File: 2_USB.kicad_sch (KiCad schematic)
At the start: 9 parts, among them J301 USB_C_Receptacle_USB2.0_16P, J302 Conn_02x03_Row_Letter_First, U301 CH224K, U302 FSUSB42MUX

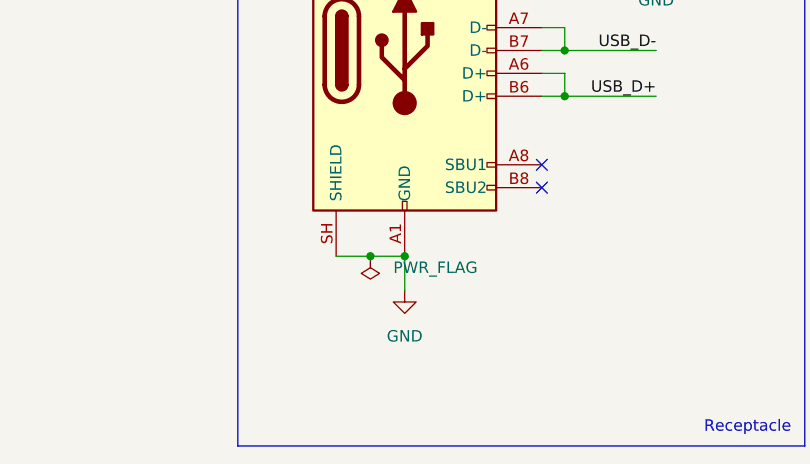
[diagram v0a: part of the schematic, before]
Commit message: Added hardware switch for active control Also added a coupling capacitor between receptacle shells and reference ground Added some more notes
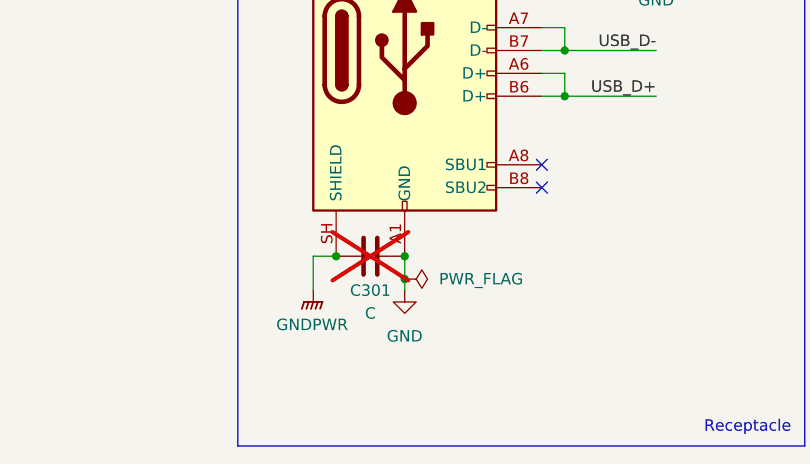
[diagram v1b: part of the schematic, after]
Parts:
- added C301: C, symbol Device:C
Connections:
- net GND: now also C301.2; no longer J301.SH (SHIELD)
- new net GNDPWR: C301.1, J301.SH (SHIELD)
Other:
- title: (none) -> Polaris/USB
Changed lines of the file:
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@@
 	(generator_version "10.0")
 	(paper "A4")
+	(title_block
+		(title "Polaris/USB")
+	)
 	(rectangle
 		(start 104.648 69.85)
@@
 			)
 		)
-	)
-	(junction
-		(at 53.34 125.73)
-		(diameter 0)
-		(color 0 0 0 0)
 	)
 	(junction
@@
 	)
 	(junction
-		(at 87.63 85.09)
+		(at 49.53 125.73)
 		(diameter 0)
 		(color 0 0 0 0)
@@
 	)
 	(junction
+		(at 87.63 85.09)
+		(diameter 0)
+		(color 0 0 0 0)
+	)
+	(junction
 		(at 144.78 128.27)
 		(diameter 0)
@@
 	)
 	(junction
+		(at 57.15 128.27)
+		(diameter 0)
+		(color 0 0 0 0)
+	)
+	(junction
 		(at 144.78 130.81)
 		(diameter 0)
@@
 	(wire
 		(pts
+			(xy 46.99 129.54) (xy 46.99 125.73)
+		)
+		(stroke
+			(width 0)
+			(type default)
+		)
+	)
+	(wire
+		(pts
+			(xy 57.15 128.27) (xy 57.15 129.54)
+		)
+		(stroke
+			(width 0)
+			(type default)
+		)
+	)
+	(wire
+		(pts
 			(xy 142.24 125.73) (xy 144.78 125.73)
 		)
@@
 	(wire
 		(pts
-			(xy 53.34 125.73) (xy 57.15 125.73)
-		)
-		(stroke
-			(width 0)
-			(type default)
-		)
-	)
-	(wire
-		(pts
 			(xy 72.39 105.41) (xy 74.93 105.41)
 		)
@@
 	(wire
 		(pts
-			(xy 49.53 125.73) (xy 53.34 125.73)
-		)
-		(stroke
-			(width 0)
-			(type default)
-		)
-	)
-	(wire
-		(pts
 			(xy 72.39 85.09) (xy 85.09 85.09)
 		)
@@
 	(wire
 		(pts
-			(xy 57.15 125.73) (xy 57.15 129.54)
+			(xy 57.15 125.73) (xy 57.15 128.27)
 		)
 		(stroke
@@
 		(pts
 			(xy 144.78 128.27) (xy 144.78 130.81)
+		)
+		(stroke
+			(width 0)
+			(type default)
+		)
+	)
+	(wire
+		(pts
+			(xy 46.99 125.73) (xy 49.53 125.73)
 		)
 		(stroke
@@
 	(symbol
 		(lib_id "power:PWR_FLAG")
-		(at 53.34 125.73 180)
+		(at 57.15 128.27 270)
 		(unit 1)
 		(body_style 1)
@@
 		(fields_autoplaced yes)
 		(property "Reference" "#FLG0302"
-			(at 53.34 127.635 0)
+			(at 59.055 128.27 0)
 			(hide yes)
 			(show_name no)
@@
 		)
 		(property "Value" "PWR_FLAG"
-			(at 55.88 126.9999 0)
-			(show_name no)
-			(do_not_autoplace no)
-			(effects
-				(font
-					(size 1.27 1.27)
-				)
-				(justify right)
+			(at 60.96 128.2699 90)
+			(show_name no)
+			(do_not_autoplace no)
+			(effects
+				(font
+					(size 1.27 1.27)
+				)
+				(justify left)
 			)
 		)
 		(property "Footprint" ""
-			(at 53.34 125.73 0)
+			(at 57.15 128.27 0)
 			(hide yes)
 			(show_name no)
@@
 		)
 		(property "Datasheet" ""
-			(at 53.34 125.73 0)
+			(at 57.15 128.27 0)
 			(hide yes)
 			(show_name no)
@@
 		)
 		(property "Description" "Special symbol for telling ERC where power comes from"
-			(at 53.34 125.73 0)
+			(at 57.15 128.27 0)
 			(hide yes)
 			(show_name no)
@@
 	)
 	(symbol
+		(lib_id "power:GNDPWR")
+		(at 46.99 129.54 0)
+		(unit 1)
+		(body_style 1)
+		(exclude_from_sim no)
+		(in_bom yes)
+		(on_board yes)
+		(in_pos_files yes)
+		(dnp no)
+		(fields_autoplaced yes)
+		(property "Reference" "#PWR0310"
+			(at 46.99 134.62 0)
+			(hide yes)
+			(show_name no)
+			(do_not_autoplace no)
+			(effects
+				(font
+					(size 1.27 1.27)
+				)
+			)
+		)
+		(property "Value" "GNDPWR"
+			(at 46.863 133.35 0)
+			(show_name no)
+			(do_not_autoplace no)
+			(effects
+				(font
+					(size 1.27 1.27)
+				)
+			)
+		)
+		(property "Footprint" ""
+			(at 46.99 130.81 0)
+			(hide yes)
+			(show_name no)
+			(do_not_autoplace no)
+			(effects
+				(font
+					(size 1.27 1.27)
+				)
+			)
+		)
+		(property "Datasheet" ""
+			(at 46.99 130.81 0)
+			(hide yes)
+			(show_name no)
+			(do_not_autoplace no)
+			(effects
+				(font
+					(size 1.27 1.27)
+				)
+			)
+		)
+		(property "Description" "Power symbol creates a global label with name \"GNDPWR\" , global ground"
+			(at 46.99 129.54 0)
+			(hide yes)
+			(show_name no)
+			(do_not_autoplace no)
+			(effects
+				(font
+					(size 1.27 1.27)
+				)
+			)
+		)
+		(pin "1"
+		)
+		(instances
+			(project "polaris"
+				(path "/cfb90e19-9fbe-47a1-a5ac-df522853d1d0/f51c22fe-6c27-4a6e-b54b-9941150cfe5c"
+					(reference "#PWR0310")
+					(unit 1)
+				)
+			)
+		)
+	)
+	(symbol
 		(lib_id "Connector_Generic:Conn_02x03_Row_Letter_First")
 		(at 217.17 130.81 90)
@@
 					(unit 1)
 				)
+			)
+		)
+	)
+	(symbol
+		(lib_id "Device:C")
+		(at 53.34 125.73 90)
+		(unit 1)
+		(body_style 1)
+		(exclude_from_sim no)
+		(in_bom yes)
+		(on_board yes)
+		(in_pos_files yes)
+		(dnp yes)
+		(property "Reference" "C301"
+			(at 53.34 129.54 90)
+			(show_name no)
+			(do_not_autoplace no)
+			(effects
+				(font
+					(size 1.27 1.27)
+				)
+			)
+		)
+		(property "Value" "C"
+			(at 53.34 132.08 90)
+			(show_name no)
+			(do_not_autoplace no)
+			(effects
+				(font
+					(size 1.27 1.27)
+				)
+			)
+		)
+		(property "Footprint" ""
+			(at 57.15 124.7648 0)
+			(hide yes)
+			(show_name no)
+			(do_not_autoplace no)
+			(effects
+				(font
+					(size 1.27 1.27)
+				)
+			)
+		)
+		(property "Datasheet" ""
+			(at 53.34 125.73 0)
+			(hide yes)
+			(show_name no)
+			(do_not_autoplace no)
+			(effects
+				(font
+					(size 1.27 1.27)
+				)
+			)
+		)
+		(property "Description" "Unpolarized capacitor"
+			(at 53.34 125.73 0)
+			(hide yes)
+			(show_name no)
+			(do_not_autoplace no)
+			(effects
+				(font
+					(size 1.27 1.27)
+				)
+			)
+		)
+		(pin "2"
+		)
+		(pin "1"
+		)
+		(instances
+			(project "polaris"
+				(path "/cfb90e19-9fbe-47a1-a5ac-df522853d1d0/f51c22fe-6c27-4a6e-b54b-9941150cfe5c"
+					(reference "C301")
+					(unit 1)
+				)

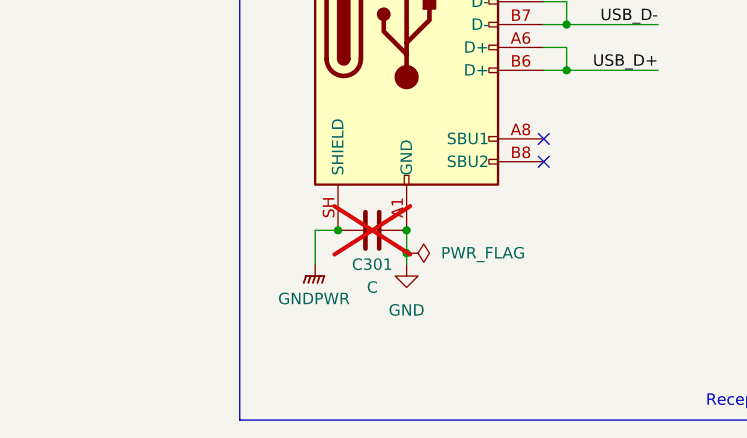
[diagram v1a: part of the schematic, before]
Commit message: Corrected grounding of shield pins in receptacles Also changed SHELL pin of microSD slot to Passive
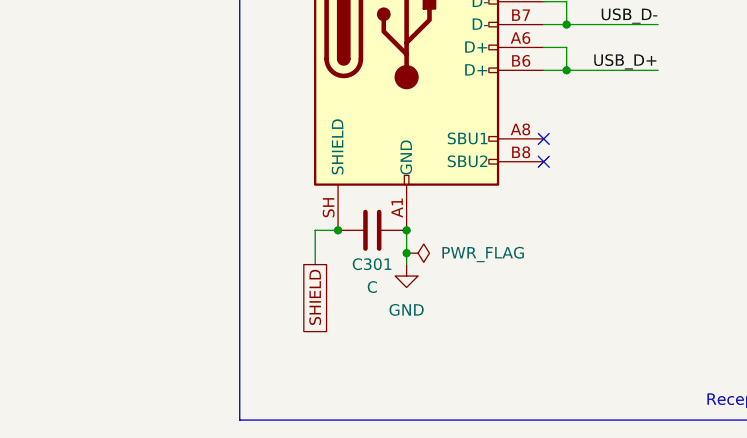
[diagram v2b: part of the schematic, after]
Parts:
- C301: now fitted
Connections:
- net GNDPWR renamed SHIELD
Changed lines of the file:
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@@
+		)
+	)
+	(global_label "SHIELD"
+		(shape passive)
+		(at 46.99 129.54 270)
+		(fields_autoplaced yes)
+		(effects
+			(font
+				(size 1.27 1.27)
+			)
+			(justify right)
+		)
+		(property "Intersheetrefs" "${INTERSHEET_REFS}"
+			(at 46.99 138.0058 90)
+			(hide yes)
+			(show_name no)
+			(do_not_autoplace no)
+			(effects
+				(font
+					(size 1.27 1.27)
+				)
+				(justify right)
+			)
 		)
 	)
@@
 	)
 	(symbol
-		(lib_id "power:GNDPWR")
-		(at 46.99 129.54 0)
-		(unit 1)
-		(body_style 1)
-		(exclude_from_sim no)
-		(in_bom yes)
-		(on_board yes)
-		(in_pos_files yes)
-		(dnp no)
-		(fields_autoplaced yes)
-		(property "Reference" "#PWR0310"
-			(at 46.99 134.62 0)
-			(hide yes)
-			(show_name no)
-			(do_not_autoplace no)
-			(effects
-				(font
-					(size 1.27 1.27)
-				)
-			)
-		)
-		(property "Value" "GNDPWR"
-			(at 46.863 133.35 0)
-			(show_name no)
-			(do_not_autoplace no)
-			(effects
-				(font
-					(size 1.27 1.27)
-				)
-			)
-		)
-		(property "Footprint" ""
-			(at 46.99 130.81 0)
-			(hide yes)
-			(show_name no)
-			(do_not_autoplace no)
-			(effects
-				(font
-					(size 1.27 1.27)
-				)
-			)
-		)
-		(property "Datasheet" ""
-			(at 46.99 130.81 0)
-			(hide yes)
-			(show_name no)
-			(do_not_autoplace no)
-			(effects
-				(font
-					(size 1.27 1.27)
-				)
-			)
-		)
-		(property "Description" "Power symbol creates a global label with name \"GNDPWR\" , global ground"
-			(at 46.99 129.54 0)
-			(hide yes)
-			(show_name no)
-			(do_not_autoplace no)
-			(effects
-				(font
-					(size 1.27 1.27)
-				)
-			)
-		)
-		(pin "1"
-		)
-		(instances
-			(project "polaris"
-				(path "/cfb90e19-9fbe-47a1-a5ac-df522853d1d0/f51c22fe-6c27-4a6e-b54b-9941150cfe5c"
-					(reference "#PWR0310")
-					(unit 1)
-				)
-			)
-		)
-	)
-	(symbol
 		(lib_id "Connector_Generic:Conn_02x03_Row_Letter_First")
 		(at 217.17 130.81 90)
@@
 		(on_board yes)
 		(in_pos_files yes)
-		(dnp yes)
+		(dnp no)
 		(property "Reference" "C301"
 			(at 53.34 129.54 90)

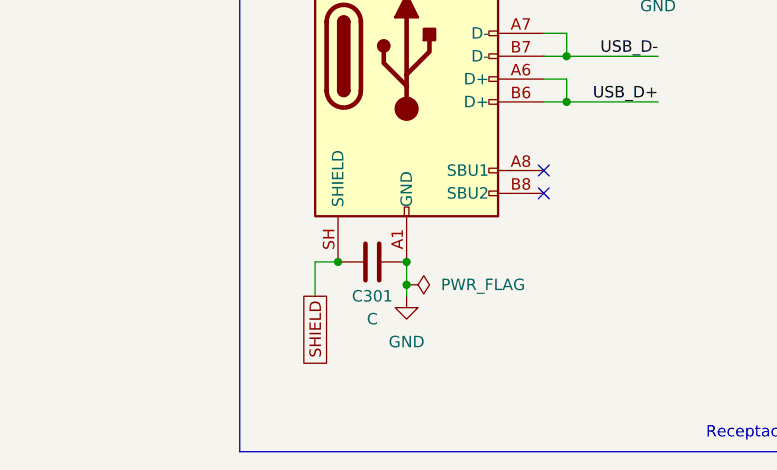
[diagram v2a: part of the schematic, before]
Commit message: Added more notes and finished footprint assignment
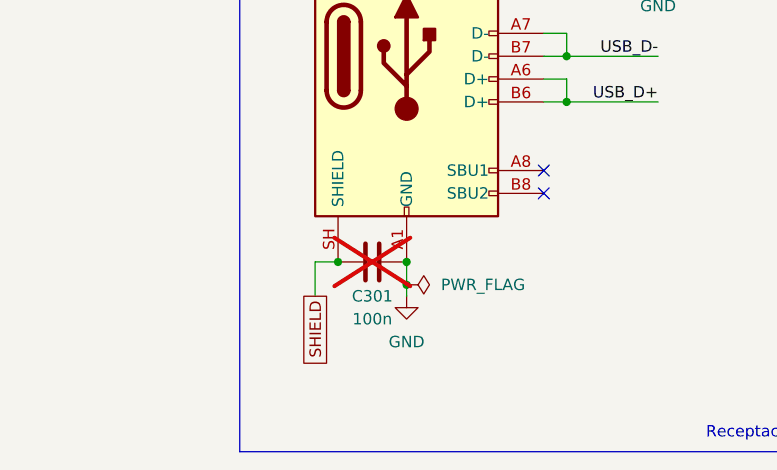
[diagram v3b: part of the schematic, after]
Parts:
- C301: value C -> 100n; footprint (none) -> Capacitor_SMD:C_0603_1608Metric; now not fitted

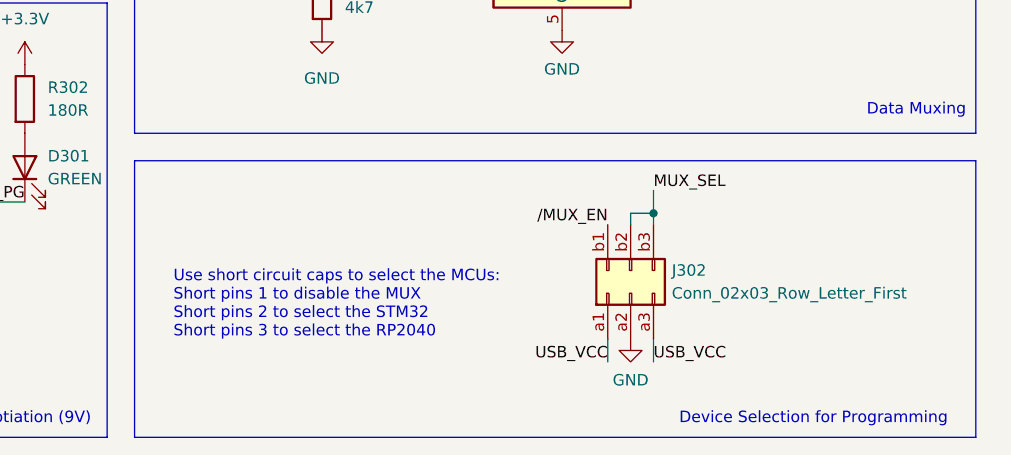
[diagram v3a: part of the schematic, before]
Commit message: Finally started the PCB layout and routing Only took me a few decades Also labeled some unlabeled nets in the schematic Changed the USB mux to be two 1x3 pin headers instead of one 2x3 Edited symbols and footprints to match pin numbers
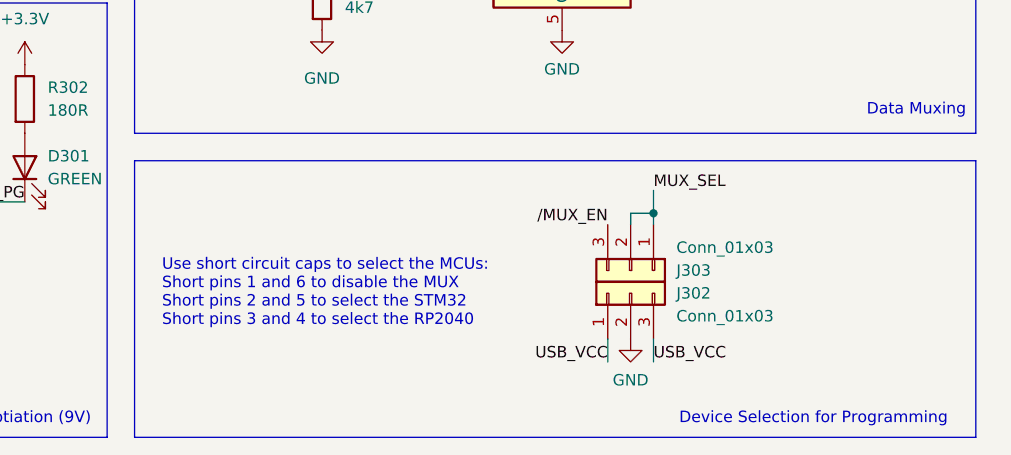
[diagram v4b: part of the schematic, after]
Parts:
- removed J302: Conn_02x03_Row_Letter_First, Connector_PinHeader_2.54mm:PinHeader_2x03_P2.54mm_Vertical, symbol Connector_Generic:Conn_02x03_Row_Letter_First
- added J302, J303: Conn_01x03, Connector_PinHeader_2.54mm:PinHeader_1x03_P2.54mm_Vertical, symbol Connector_Generic:Conn_01x03
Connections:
- net GND: now also J302.2 (Pin_2)
- net MUX_SEL: now also J303.1 (Pin_1), J303.2 (Pin_2)
- net USB_VCC: now also J302.1 (Pin_1), J302.3 (Pin_3)
- net /MUX_EN: now also J303.3 (Pin_3)
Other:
- note added: "Use short circuit caps to select the MCUs: Short pins 1 and 6 to disable the MUX Short pins 2 and 5 to select the STM32 Short pins 3 and 4 to select the RP2040"
- note removed: "Use short circuit caps to select the MCUs: Short pins 1 to disable the MUX Short pins 2 to select the STM32 Short pins 3 to select the RP2040"
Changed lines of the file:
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@@
 		)
 	)
-	(text "Use short circuit caps to select the MCUs:\nShort pins 1 to disable the MUX\nShort pins 2 to select the STM32\nShort pins 3 to select the RP2040\n"
+	(text "Use short circuit caps to select the MCUs:\nShort pins 1 and 6 to disable the MUX\nShort pins 2 and 5 to select the STM32\nShort pins 3 and 4 to select the RP2040\n"
 		(exclude_from_sim no)
-		(at 166.37 132.08 0)
+		(at 165.1 130.81 0)
 		(effects
 			(font
@@
 	)
 	(symbol
+		(lib_id "Connector_Generic:Conn_01x03")
+		(at 217.17 128.27 270)
+		(unit 1)
+		(body_style 1)
+		(exclude_from_sim no)
+		(in_bom yes)
+		(on_board yes)
+		(in_pos_files yes)
+		(dnp no)
+		(property "Reference" "J303"
+			(at 222.25 128.27 90)
+			(show_name no)
+			(do_not_autoplace no)
+			(effects
+				(font
+					(size 1.27 1.27)
+				)
+				(justify left)
+			)
+		)
+		(property "Value" "Conn_01x03"
+			(at 222.25 125.73 90)
+			(show_name no)
+			(do_not_autoplace no)
+			(effects
+				(font
+					(size 1.27 1.27)
+				)
+				(justify left)
+			)
+		)
+		(property "Footprint" "Connector_PinHeader_2.54mm:PinHeader_1x03_P2.54mm_Vertical"
+			(at 217.17 128.27 0)
+			(hide yes)
+			(show_name no)
+			(do_not_autoplace no)
+			(effects
+				(font
+					(size 1.27 1.27)
+				)
+			)
+		)
+		(property "Datasheet" ""
+			(at 217.17 128.27 0)
+			(hide yes)
+			(show_name no)
+			(do_not_autoplace no)
+			(effects
+				(font
+					(size 1.27 1.27)
+				)
+			)
+		)
+		(property "Description" "Generic connector, single row, 01x03, script generated (kicad-library-utils/schlib/autogen/connector/)"
+			(at 217.17 128.27 0)
+			(hide yes)
+			(show_name no)
+			(do_not_autoplace no)
+			(effects
+				(font
+					(size 1.27 1.27)
+				)
+			)
+		)
+		(pin "2"
+		)
+		(pin "3"
+		)
+		(pin "1"
+		)
+		(instances
+			(project "polaris"
+				(path "/cfb90e19-9fbe-47a1-a5ac-df522853d1d0/f51c22fe-6c27-4a6e-b54b-9941150cfe5c"
+					(reference "J303")
+					(unit 1)
+				)
+			)
+		)
+	)
+	(symbol
 		(lib_id "Device:R")
 		(at 182.88 97.79 0)
@@
 	)
 	(symbol
-		(lib_id "Connector_Generic:Conn_02x03_Row_Letter_First")
+		(lib_id "Connector_Generic:Conn_01x03")
 		(at 217.17 130.81 90)
 		(unit 1)
@@
 		(in_pos_files yes)
 		(dnp no)
-		(fields_autoplaced yes)
 		(property "Reference" "J302"
-			(at 221.742 128.2699 90)
+			(at 222.25 130.81 90)
 			(show_name no)
 			(do_not_autoplace no)
@@
 			)
 		)
-		(property "Value" "Conn_02x03_Row_Letter_First"
-			(at 221.742 130.8099 90)
+		(property "Value" "Conn_01x03"
+			(at 222.25 133.35 90)
 			(show_name no)
 			(do_not_autoplace no)
@@
 			)
 		)
-		(property "Footprint" "Connector_PinHeader_2.54mm:PinHeader_2x03_P2.54mm_Vertical"
+		(property "Footprint" "Connector_PinHeader_2.54mm:PinHeader_1x03_P2.54mm_Vertical"
 			(at 217.17 130.81 0)
 			(hide yes)
@@
 			)
 		)
-		(property "Description" "Generic connector, double row, 02x03, row letter first pin numbering scheme (pin number consists of a letter for the row and a number for the pin index in this row. a1, ..., aN; b1, ..., bN), script generated (kicad-library-utils/schlib/autogen/connector/)"
+		(property "Description" "Generic connector, single row, 01x03, script generated (kicad-library-utils/schlib/autogen/connector/)"
 			(at 217.17 130.81 0)
 			(hide yes)
@@
 			)
 		)
-		(property "Description_1" ""
-			(at 217.17 130.81 90)
-			(hide yes)
-			(show_name no)
-			(do_not_autoplace no)
-			(effects
-				(font
-					(size 1.27 1.27)
-				)
-			)
-		)
-		(property "KLC_S3.3" ""
-			(at 217.17 130.81 90)
-			(hide yes)
-			(show_name no)
-			(do_not_autoplace no)
-			(effects
-				(font
-					(size 1.27 1.27)
-				)
-			)
-		)
-		(property "KLC_S4.1" ""
-			(at 217.17 130.81 90)
-			(hide yes)
-			(show_name no)
-			(do_not_autoplace no)
-			(effects
-				(font
-					(size 1.27 1.27)
-				)
-			)
-		)
-		(property "KLC_S4.2_DVDD" ""
-			(at 217.17 130.81 90)
-			(hide yes)
-			(show_name no)
-			(do_not_autoplace no)
-			(effects
-				(font
-					(size 1.27 1.27)
-				)
-			)
-		)
-		(property "KLC_S4.2_VREG_VOUT" ""
-			(at 217.17 130.81 90)
-			(hide yes)
-			(show_name no)
-			(do_not_autoplace no)
-			(effects
-				(font
-					(size 1.27 1.27)
-				)
-			)
-		)
-		(property "LCSC Part Name" ""
-			(at 217.17 130.81 90)
-			(hide yes)
-			(show_name no)
-			(do_not_autoplace no)
-			(effects
-				(font
-					(size 1.27 1.27)
-				)
-			)
-		)
-		(property "Manufacturer Part" ""
-			(at 217.17 130.81 90)
-			(hide yes)
-			(show_name no)
-			(do_not_autoplace no)
-			(effects
-				(font
-					(size 1.27 1.27)
-				)
-			)
-		)
-		(property "Supplier" ""
-			(at 217.17 130.81 90)
-			(hide yes)
-			(show_name no)
-			(do_not_autoplace no)
-			(effects
-				(font
-					(size 1.27 1.27)
-				)
-			)
-		)
-		(property "Supplier Part" ""
-			(at 217.17 130.81 90)
-			(hide yes)
-			(show_name no)
-			(do_not_autoplace no)
-			(effects
-				(font
-					(size 1.27 1.27)
-				)
-			)
-		)
-		(pin "b1"
-		)
-		(pin "a3"
-		)
-		(pin "a2"
-		)
-		(pin "b2"
-		)
-		(pin "b3"
-		)
-		(pin "a1"
+		(pin "1"
+		)
+		(pin "2"
+		)
+		(pin "3"
 		)
 		(instances
